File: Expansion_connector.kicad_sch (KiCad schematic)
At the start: 1 part, among them J10 ASP-218650-01_mounting_holes

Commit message: [#82057] Reorganise FMC+ pins so that they obey standard
[#82057] Add passives to expansion connector

[#82055] Clean up
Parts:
- added C115, C116, C117, C118: C_100n_50V_X8L_0402, antmicro-footprints:C_0402_1005Metric, symbol antmicroCapacitors0402:C_100n_50V_X8L_0402
- added C119, C120, C121, C122, C123, C124, C125, C126, C127, C128, C129, C130, C131, C132, C133, C134: C_220n_6V3_X7R_0402, antmicro-footprints:C_0402_1005Metric, symbol antmicroCapacitors0402:C_220n_6V3_X7R_0402
- added R115, R116, R126, R82: R_0R_22.4A_0603, antmicro-footprints:R_0603_1608Metric, symbol antmicroResistors0603:R_0R_22.4A_0603
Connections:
- net RGMII.MDC is gone; now on net GND: J10.M20
- net RGMII.RD1 is gone; now on net GND: J10.M29
- net RGMII.RD2 is gone; now on net GND: J10.M32
- net RGMII.TD3 is gone; now on net GND: J10.M17
- net CAN0.DIN: now also J10.A10; no longer J10.K32
- net CAN0.DOUT: now also J10.A11; no longer J10.K33
- net CAN1.DIN: now also J10.A14; no longer J10.K36
- net CAN1.DOUT: now also J10.A15; no longer J10.K37
- net GND: now also J10.B02, J10.B03, J10.B10, J10.B11, J10.B14, J10.B15, J10.B18, J10.B22, J10.B23, J10.B26, J10.B27, J10.B30, J10.B31, J10.B38, J10.B39, J10.C04, J10.C05, J10.C09, J10.C12, J10.C16, J10.C17, J10.C29, J10.C32, J10.C36, J10.C38, J10.D02, J10.D03, J10.D07, J10.D10, J10.D13, J10.D16, J10.D25, J10.D28, J10.D37, J10.D39, J10.E01, J10.E04, J10.E08, J10.E11, J10.E17, J10.E23, J10.E26, J10.E35, J10.E38, J10.F09, J10.F12, J10.F21, J10.F24, J10.F33, J10.F36, J10.G11, J10.G14, J10.G23, J10.G26, J10.G35, J10.G38, J10.H09, J10.H12, J10.H21, J10.H24, J10.H33, J10.H36, J10.J11, J10.J14, J10.J23, J10.J26, J10.J35, J10.J38, J10.K09, J10.K12, J10.K21, J10.K24, J10.K33, J10.K36, J10.L02, J10.L03, J10.L06, J10.L07, J10.L10, J10.L11, J10.L14, J10.L15, J10.L18, J10.L19, J10.L22, J10.L23, J10.L26, J10.L27, J10.L30, J10.L31, J10.L34, J10.L35, J10.L38, J10.L39, J10.M01, J10.M04, J10.M05, J10.M08, J10.M09, J10.M12, J10.M13, J10.M16, J10.M21, J10.M24, J10.M25, J10.M28, J10.M33, J10.M36, J10.M37, J10.M40, C115.1, C116.1, C117.1, C118.1; no longer J10.B12, J10.B13, J10.B20, J10.B28, J10.B29, J10.C02, J10.C07, J10.C14, J10.C34, J10.C39, J10.D05, J10.D11, J10.D12, J10.D18, J10.D23, J10.E06, J10.E13, J10.E21, J10.E24, J10.E25, J10.E28, J10.E33, J10.E36, J10.E37, J10.F07, J10.F10, J10.F11, J10.F14, J10.F19, J10.F22, J10.F23, J10.F26, J10.F31, J10.F34, J10.F35, J10.F38, J10.G09, J10.G12, J10.G13, J10.G16, J10.G21, J10.G24, J10.G25, J10.G28, J10.G33, J10.G36, J10.G37, J10.H02, J10.H07, J10.H10, J10.H11, J10.H14, J10.H19, J10.H22, J10.H23, J10.H26, J10.H31, J10.H34, J10.H35, J10.H38, J10.J09, J10.J12, J10.J13, J10.J16, J10.J21, J10.J24, J10.J25, J10.J28, J10.J33, J10.J36, J10.J37, J10.K07, J10.K10, J10.K11, J10.K14, J10.K19, J10.K22, J10.K23, J10.K26, J10.K31, J10.K34, J10.K35, J10.K38, J10.L01, J10.L04, J10.L05, J10.L08, J10.L09, J10.L12, J10.L13, J10.L16, J10.L17, J10.L20, J10.L21, J10.L24, J10.L25, J10.L28, J10.L29, J10.L32, J10.L33, J10.L36, J10.L37, J10.L40, J10.M02, J10.M03, J10.M06, J10.M07, J10.M10, J10.M11, J10.M14, J10.M15, J10.M18, J10.M19, J10.M22, J10.M23, J10.M26, J10.M27, J10.M30, J10.M31, J10.M34, J10.M35, J10.M38, J10.M39
- net GPIO.04: now also J10.H29; no longer J10.E10
- net GPIO.05: now also J10.H28; no longer J10.E09
- net GPIO.08: now also J10.H35; no longer J10.E16
- net GPIO.09: now also J10.H34; no longer J10.E15
- net GPIO.13: now also J10.H32; no longer J10.E12
- net GPIO.14: now also J10.H31; no longer J10.E11
- net GPIO.15: now also J10.H38; no longer J10.E18
- net GPIO.16: now also J10.H37; no longer J10.E17
- net GPIO.20: now also J10.H26; no longer J10.E08
- net GPIO.21: now also J10.H25; no longer J10.E07
- net GPIO.MCLK01: now also J10.G02; no longer J10.C15
- net GPIO.MCLK02: now also J10.G03; no longer J10.C16
- net GPIO.MCLK03: now also J10.H04; no longer J10.C17
- net GPIO.MCLK04: now also J10.H05; no longer J10.C18
- net GPIO.MCLK05: now also J10.H07; no longer J10.C19
- net GPIO.USER_BTN0: now also J10.H22; no longer J10.E03
- net GPIO.USER_BTN1: now also J10.H23; no longer J10.E04
- net GPIO.USER_LED0: now also J10.H19; no longer J10.E01
- net GPIO.USER_LED1: now also J10.H20; no longer J10.E02
- net I2S2.CLK: now also J10.G18; no longer J10.C03
- net I2S2.FS: now also J10.G19; no longer J10.C04
- net I2S2.SDIN: now also J10.G22; no longer J10.C06
- net I2S2.SDOUT: now also J10.G21; no longer J10.C05
- net I2S3.CLK: now also J10.G24; no longer J10.C09
- net I2S3.FS: now also J10.G25; no longer J10.C10
- net I2S3.SDIN: now also J10.G28; no longer J10.C12
- net I2S3.SDOUT: now also J10.G27; no longer J10.C11
- net PCIe_{C5x8}.CK+: now also J10.Z21
- net PCIe_{C5x8}.CK-: now also J10.Z20
- net PCIe_{C5x8}.RX0+: now also J10.Z08
- net PCIe_{C5x8}.RX0-: now also J10.Z09
- net PCIe_{C5x8}.RX1+: now also J10.Z12
- net PCIe_{C5x8}.RX1-: now also J10.Z13
- net PCIe_{C5x8}.RX2+: now also J10.Z16
- net PCIe_{C5x8}.RX2-: now also J10.Z17
- net PCIe_{C5x8}.RX3+: now also J10.Z24
- net PCIe_{C5x8}.RX3-: now also J10.Z25
- net PCIe_{C5x8}.RX4+: now also J10.Z28
- net PCIe_{C5x8}.RX4-: now also J10.Z29
- net PCIe_{C5x8}.RX5+: now also J10.Z32
- net PCIe_{C5x8}.RX5-: now also J10.Z33
- net PCIe_{C5x8}.RX6+: now also J10.Z36
- net PCIe_{C5x8}.RX6-: now also J10.Z37
- net PCIe_{C5x8}.RX7+: now also J10.A03
- net PCIe_{C5x8}.RX7-: now also J10.A02
- net PCIe_{C5x8}.TX0+: now also C119.1
- net PCIe_{C5x8}.TX0-: now also C125.1
- net PCIe_{C5x8}.TX1+: now also C120.1
- net PCIe_{C5x8}.TX1-: now also C121.1
- net PCIe_{C5x8}.TX2+: now also C122.1
- net PCIe_{C5x8}.TX2-: now also C123.1
- net PCIe_{C5x8}.TX3+: now also C124.1
- net PCIe_{C5x8}.TX3-: now also C126.1
- net PCIe_{C5x8}.TX4+: now also C127.1
- net PCIe_{C5x8}.TX4-: now also C128.1
- net PCIe_{C5x8}.TX5+: now also C129.1
- net PCIe_{C5x8}.TX5-: now also C130.1
- net PCIe_{C5x8}.TX6+: now also C131.1
- net PCIe_{C5x8}.TX6-: now also C132.1
- net PCIe_{C5x8}.TX7+: now also C133.1
- net PCIe_{C5x8}.TX7-: now also C134.1
- net PCIe_{C5x8}.~{CLKREQ}: now also J10.A07
- net PCIe_{C5x8}.~{RST}: now also J10.A06
- net RGMII.MDIO: now also J10.E15; no longer J10.M21
- net RGMII.RD0: now also J10.E22; no longer J10.M28
- net RGMII.RD3: now also J10.E27; no longer J10.M33
- net RGMII.RXC: now also J10.E19; no longer J10.M25
- net RGMII.RX_CTL: now also J10.E18; no longer J10.M24
- net RGMII.TD0: now also J10.E06; no longer J10.M12
- net RGMII.TD1: now also J10.E07; no longer J10.M13
- net RGMII.TD2: now also J10.E10; no longer J10.M16
- net RGMII.TXC: now also J10.E03; no longer J10.M09
- net RGMII.TX_CTL: now also J10.E02; no longer J10.M08
- net RGMII.~{INT}: now also J10.E31; no longer J10.M37
- net RGMII.~{RST}: now also J10.E30; no longer J10.M36
- net SDIO.CD/GPIO02: now also J10.G07; no longer J10.L27
- net SDIO.CLK: now also J10.G16; no longer J10.L39
- net SDIO.CMD: now also J10.G15; no longer J10.L38
- net SDIO.D0: now also J10.G13; no longer J10.L35
- net SDIO.D1: now also J10.G12; no longer J10.L34
- net SDIO.D2: now also J10.G10; no longer J10.L31
- net SDIO.D3: now also J10.G09; no longer J10.L30
- net SDIO.WP/GPIO29: now also J10.G06; no longer J10.L26
- net SPI1.MISO: now also J10.F19; no longer J10.B04
- net SPI1.MOSI: now also J10.F20; no longer J10.B05
- net SPI1.SCK: now also J10.F22; no longer J10.B03
- net SPI1.~{CS0}: now also J10.F16; no longer J10.B01
- net SPI1.~{CS1}: now also J10.F17; no longer J10.B02
- net SPI2.MISO: now also J10.F28; no longer J10.B10
- net SPI2.MOSI: now also J10.F29; no longer J10.B11
- net SPI2.SCK: now also J10.F26; no longer J10.B09
- net SPI2.~{CS0}: now also J10.F25; no longer J10.B08
- net SPI3.MISO: now also J10.F34; no longer J10.B17
- net SPI3.MOSI: now also J10.F35; no longer J10.B18
- net SPI3.SCK: now also J10.F37; no longer J10.B16
- net SPI3.~{CS0}: now also J10.F31; no longer J10.B14
- net SPI3.~{CS1}: now also J10.F32; no longer J10.B15
- net UART2.CTS: now also J10.D09; no longer J10.D02
- net UART2.RTS: now also J10.D08; no longer J10.D01
- net UART2.RX: now also J10.D12; no longer J10.D04
- net UART2.TX: now also J10.D11; no longer J10.D03
- net UART4.CTS: now also J10.D15; no longer J10.D08
- net UART4.RTS: now also J10.D14; no longer J10.D07
- net UART4.RX: now also J10.D18; no longer J10.D10
- net UART4.TX: now also J10.D17; no longer J10.D09
- net UART5.CTS: now also J10.D21; no longer J10.D14
- net UART5.RTS: now also J10.D20; no longer J10.D13
- net UART5.RX: now also J10.D24; no longer J10.D16
- net UART5.TX: now also J10.D23; no longer J10.D15
- net +5V_CONN: now reaches J10.G39
- net +5V_CONN: now also J10.H40, C118.2, R126.2
- net +1V8_CONN: now reaches J10.E39
- net +1V8_CONN: now also J10.F40, C115.2, R82.2
- net +12V_CONN: now reaches J10.C35
- net +12V_CONN: now also J10.C37, J10.L36, J10.L37, J10.L40, C117.2, R116.2
- net +3V3_CONN: now reaches J10.D36
- net +3V3_CONN: now also J10.C39, J10.D38, J10.D40, J10.Z40, C116.2, R115.2
- net PET0_P: now reaches J10.Y10
- net PET0_P: now also C119.2
- net PET0_N: now reaches J10.Y11
- net PET0_N: now also C125.2
- net PET1_P: now reaches J10.Y14
- net PET1_P: now also C120.2
- net PET1_N: now reaches J10.Y15
- net PET1_N: now also C121.2
- net PET2_P: now reaches J10.Y18
- net PET2_P: now also C122.2
- net PET2_N: now reaches J10.Y19
- net PET2_N: now also C123.2
- net PET3_P: now reaches J10.Y22
- net PET3_P: now also C124.2
- net PET3_N: now reaches J10.Y23
- net PET3_N: now also C126.2
- net PET4_P: now reaches J10.Y26
- net PET4_P: now also C127.2
- net PET4_N: now reaches J10.Y27
- net PET4_N: now also C128.2
- net PET5_P: now reaches J10.Y30
- net PET5_P: now also C129.2
- net PET5_N: now reaches J10.Y31
- net PET5_N: now also C130.2
- net PET6_P: now reaches J10.Y34
- net PET6_P: now also C131.2
- net PET6_N: now reaches J10.Y35
- net PET6_N: now also C132.2
- net PET7_P: now reaches J10.Y38
- net PET7_P: now also C133.2
- net PET7_N: now reaches J10.Y39
- net PET7_N: now also C134.2
- new net +12V: R116.1
- new net +1V8: R82.1
- new net +3V3: R115.1
- new net +5V: R126.1
- no-connect marks 0 -> 168
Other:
- note added: "FMC+ expansion connector"
- note added: "How many blades do we need for enough power For future for Jetson AGX Thor it was discussed we need 150W but for Jetson AGX Orin 100W currnet ratin per pin 9.8A, for 12V we need two blades for it."
- note removed: "Currnet rating 2.7A 339VDC"
- moved on the sheet: J10A, J10B, J10C, J10D, J10E, J10F, J10G

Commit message: [#82757] Rename project to jetson-agx-thor-baseboard
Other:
- title: Jetson Orin AGX Baseboard -> Jetson AGX Thor Baseboard
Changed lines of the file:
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@@
 	(paper "A3")
 	(title_block
-		(title "Jetson Orin AGX Baseboard")
+		(title "Jetson AGX Thor Baseboard")
 		(date "2025-08-11")
 		(rev "1.0.0")

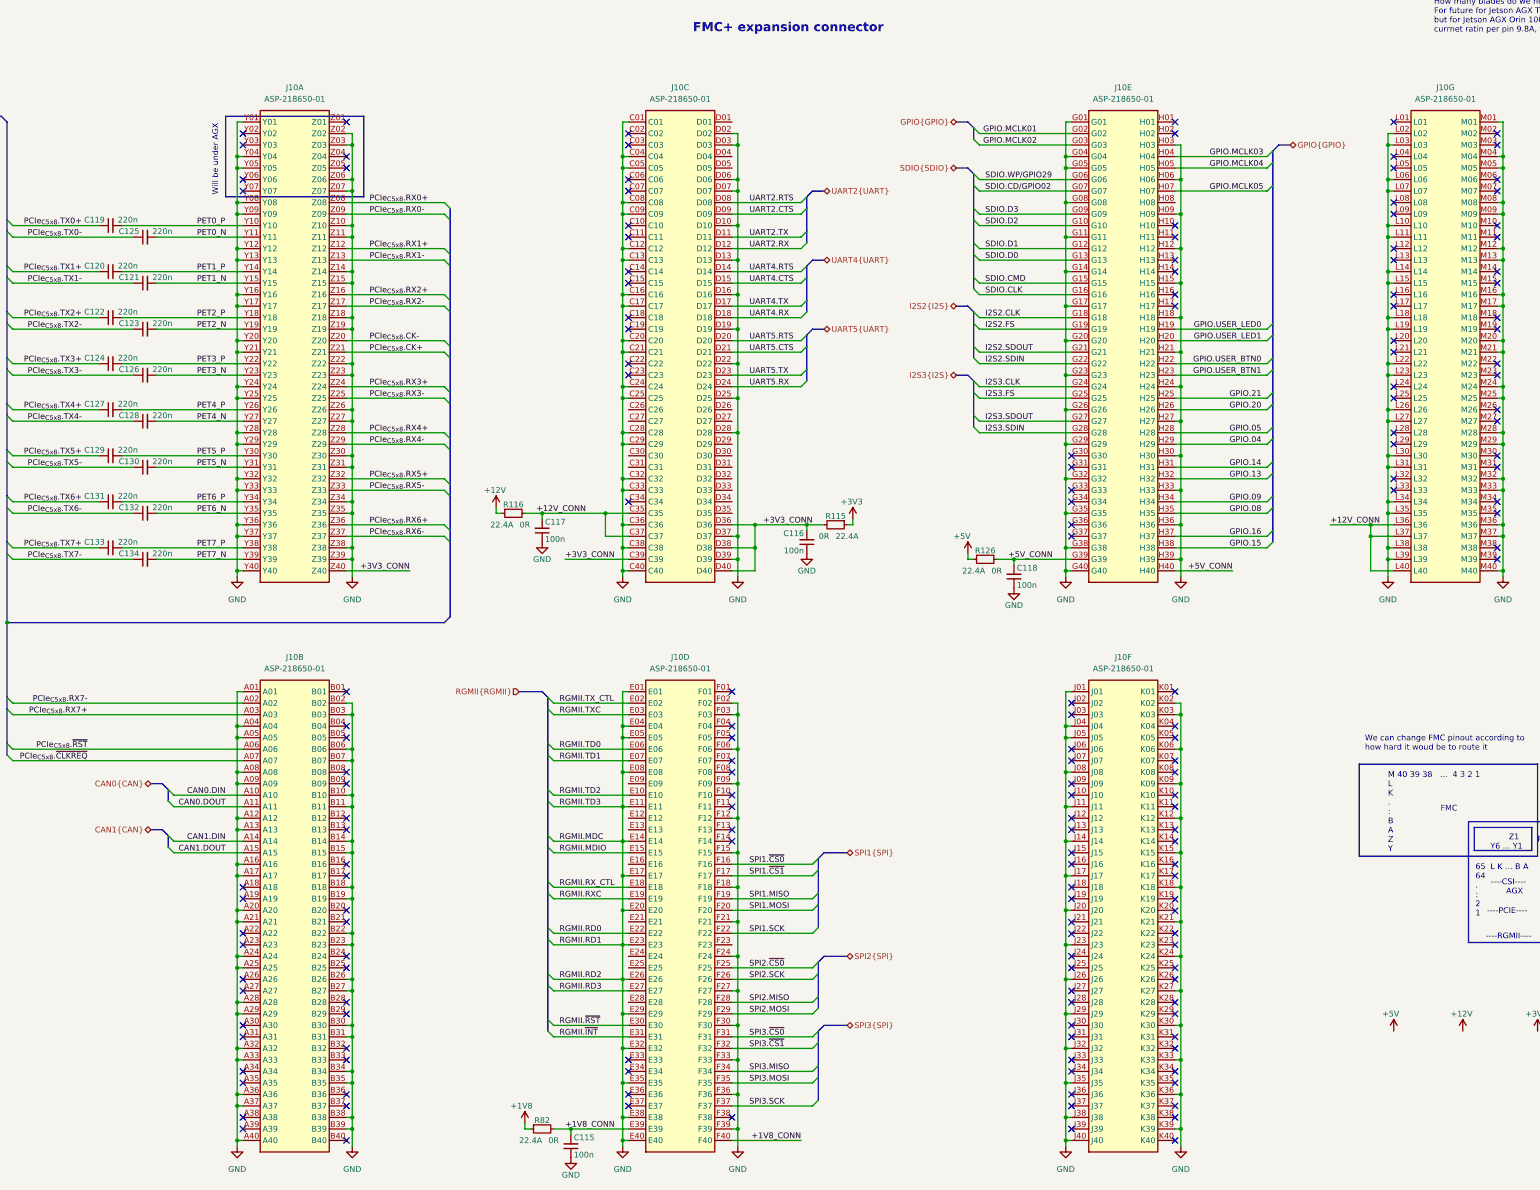
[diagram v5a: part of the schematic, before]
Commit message: [#82757] Cleanup: reorganise page numbers and fix annotations
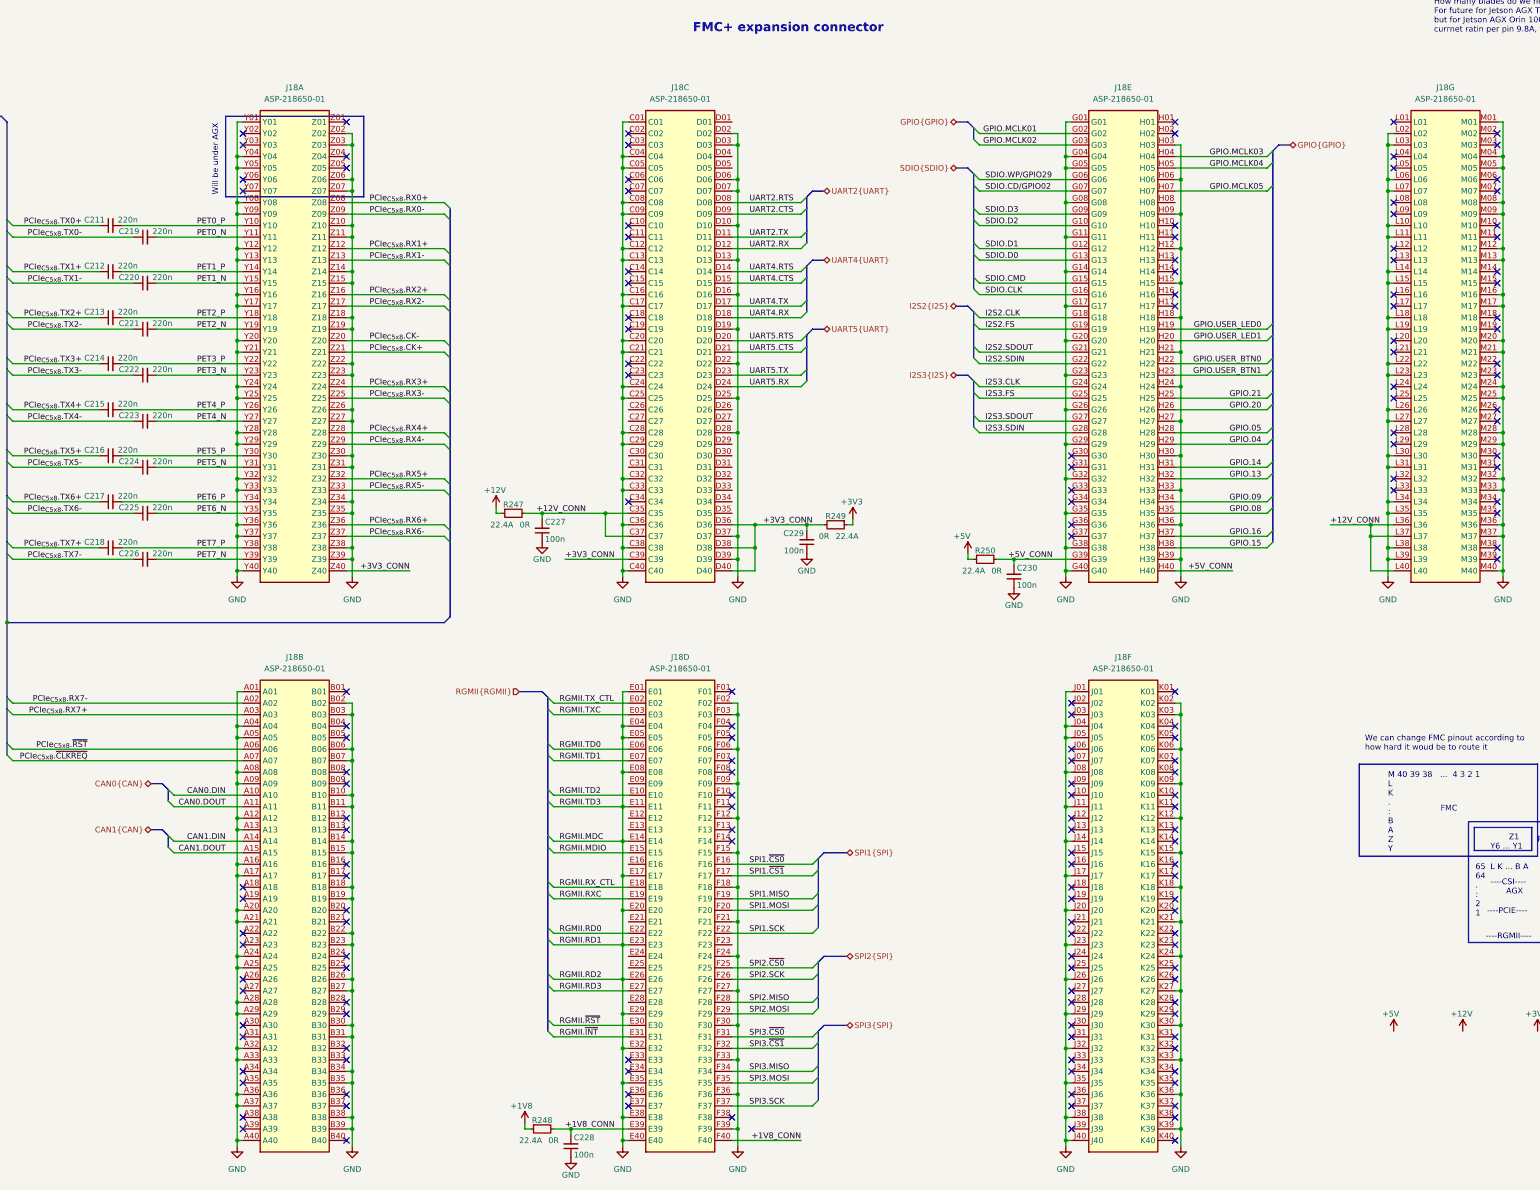
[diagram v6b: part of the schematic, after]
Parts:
- renumbered C119 to C211, C120 to C212, C122 to C213, C124 to C214, C127 to C215, C129 to C216, C131 to C217, C133 to C218, C125 to C219, C121 to C220, C123 to C221, C126 to C222, C128 to C223, C130 to C224, C132 to C225, C134 to C226, C117 to C227, C115 to C228, C116 to C229, C118 to C230, J10 to J18, R116 to R247, R82 to R248, R115 to R249, R126 to R250
